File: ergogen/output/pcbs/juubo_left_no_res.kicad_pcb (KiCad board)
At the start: 2 copper layers, 145.6 x 125.5 mm, 40 parts

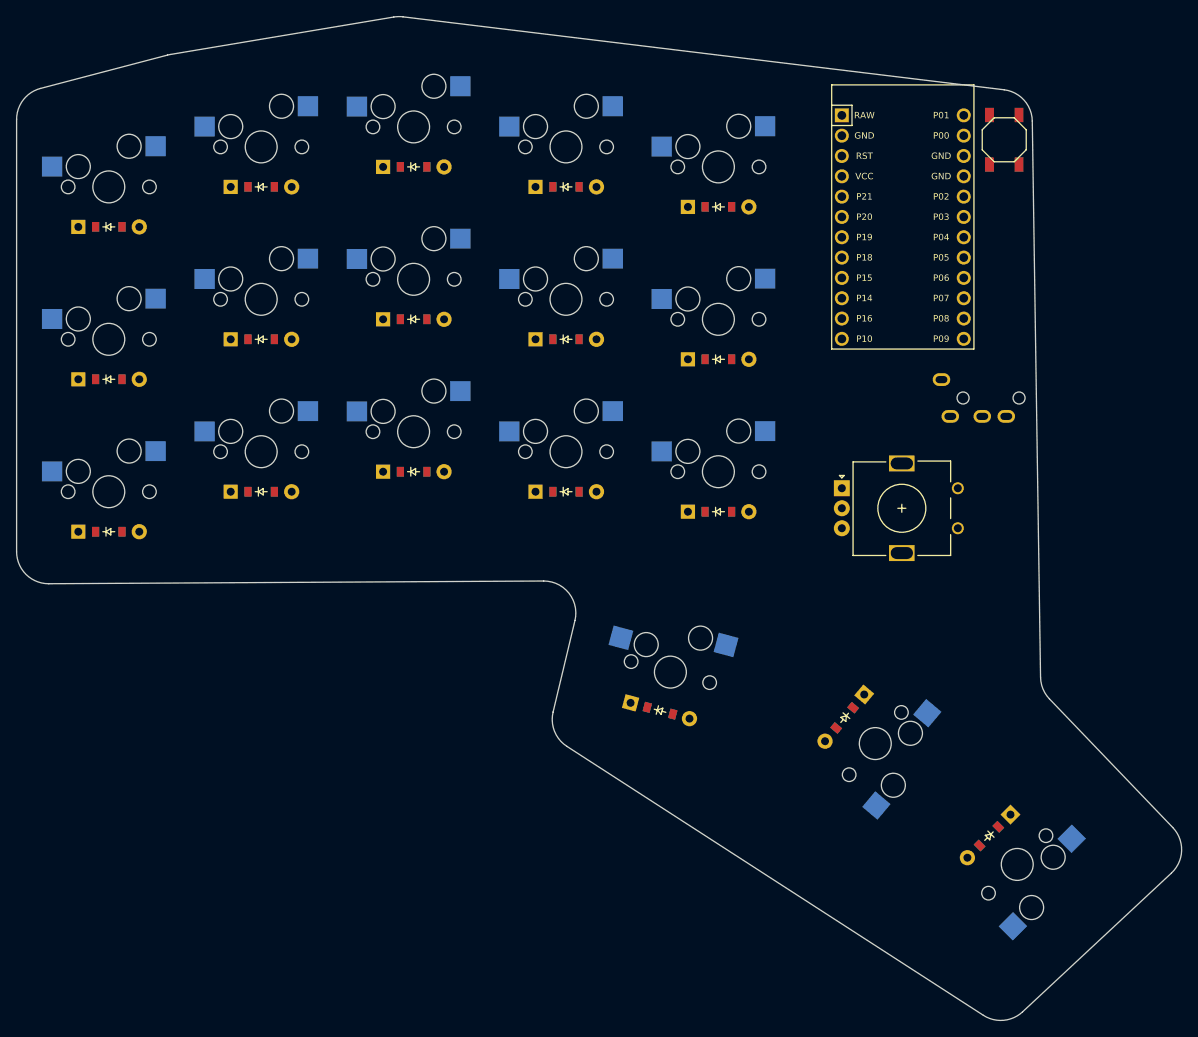
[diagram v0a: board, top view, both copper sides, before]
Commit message: Add mounting holes to ergogen-generated pcb
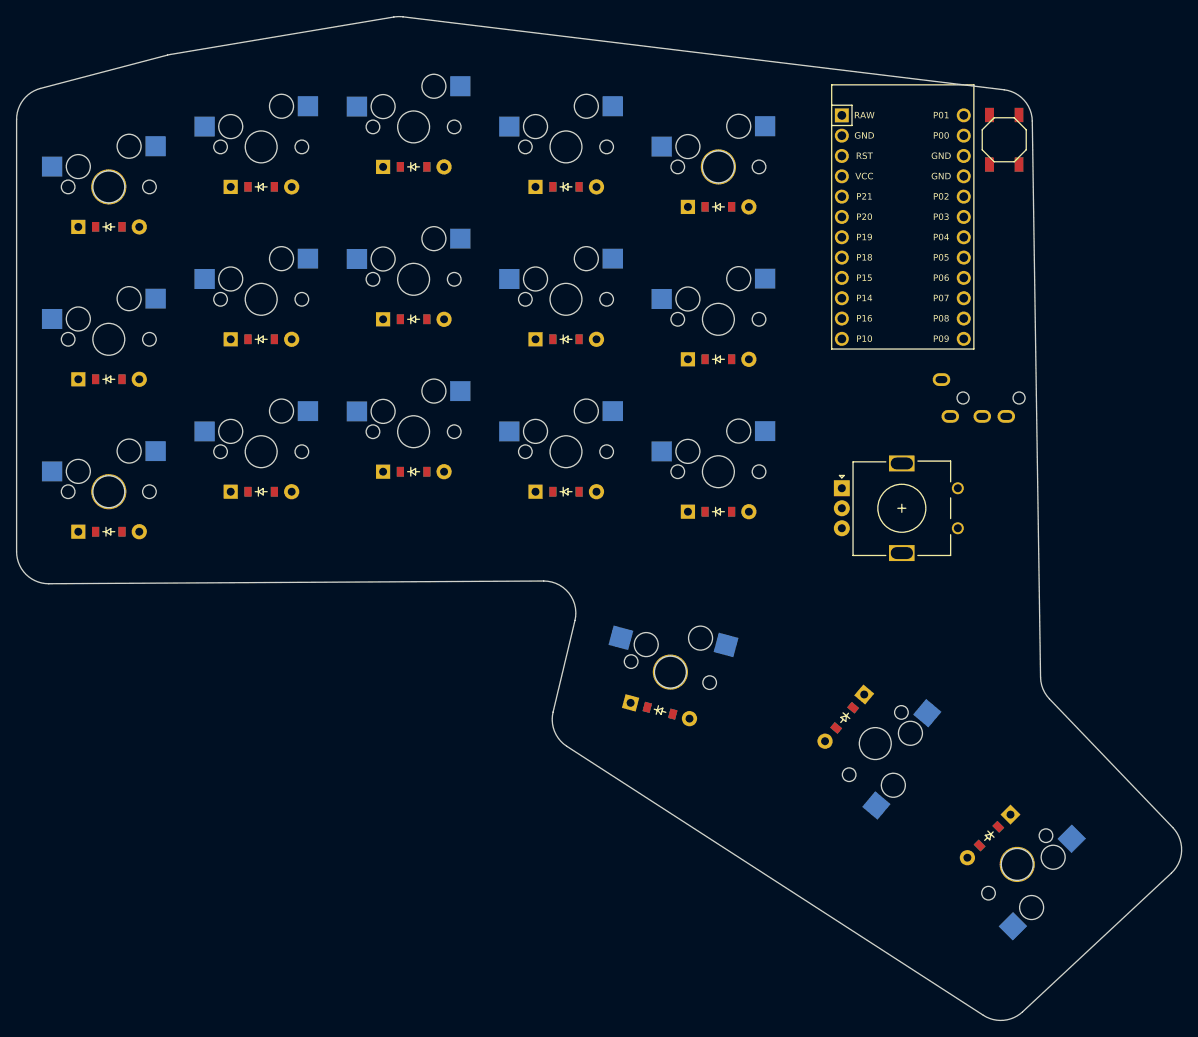
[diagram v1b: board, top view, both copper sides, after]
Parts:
- added _1: , MountingHole_2.2mm_M2_Pad_Via, F.Cu at (100.0, 61.9)
- added _2: , MountingHole_2.2mm_M2_Pad_Via, F.Cu at (176.2, 59.4)
- added _3: , MountingHole_2.2mm_M2_Pad_Via, F.Cu at (100.0, 100.0)
- added _4: , MountingHole_2.2mm_M2_Pad_Via, F.Cu at (170.2, 122.5)
- added _5: , MountingHole_2.2mm_M2_Pad_Via, F.Cu at (213.6, 146.6)
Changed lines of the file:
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@@
         (pad 4 thru_hole oval (at 0 3.2 -90) (size 1.6 2.2) (drill oval 0.9 1.5) (layers *.Cu *.Mask) (net 2 "GND"))
       )
+    (module "MountingHole_2.2mm_M2_Pad_Via" (version 20210722) (generator pcbnew) (layer "F.Cu")
+      (at 100 61.900000000000006 0)
+      (fp_text reference "_1" (at 0 -3.2) (layer "F.SilkS") hide
+        (effects (font (size 1 1) (thickness 0.15)))
+      )
+      (fp_circle (center 0 0) (end 2.45 0) (layer "F.CrtYd") (width 0.05) (fill none))
+      (pad "1" thru_hole circle locked (at 1.166726 1.166726) (size 0.7 0.7) (drill 0.4) (layers *.Cu *.Mask))
+      (pad "1" thru_hole circle locked (at 0 0) (size 4.4 4.4) (drill 2.2) (layers *.Cu *.Mask))
+      (pad "1" thru_hole circle locked (at 0 1.65) (size 0.7 0.7) (drill 0.4) (layers *.Cu *.Mask))
+      (pad "1" thru_hole circle locked (at 1.166726 -1.166726) (size 0.7 0.7) (drill 0.4) (layers *.Cu *.Mask))
+      (pad "1" thru_hole circle locked (at -1.65 0) (size 0.7 0.7) (drill 0.4) (layers *.Cu *.Mask))
+      (pad "1" thru_hole circle locked (at -1.166726 -1.166726) (size 0.7 0.7) (drill 0.4) (layers *.Cu *.Mask))
+      (pad "1" thru_hole circle locked (at -1.166726 1.166726) (size 0.7 0.7) (drill 0.4) (layers *.Cu *.Mask))
+      (pad "1" thru_hole circle locked (at 1.65 0) (size 0.7 0.7) (drill 0.4) (layers *.Cu *.Mask))
+      (pad "1" thru_hole circle locked (at 0 -1.65) (size 0.7 0.7) (drill 0.4) (layers *.Cu *.Mask))
+    )
+    (module "MountingHole_2.2mm_M2_Pad_Via" (version 20210722) (generator pcbnew) (layer "F.Cu")
+      (at 176.2 59.400000000000006 0)
+      (fp_text reference "_2" (at 0 -3.2) (layer "F.SilkS") hide
+        (effects (font (size 1 1) (thickness 0.15)))
+      )
+      (fp_circle (center 0 0) (end 2.45 0) (layer "F.CrtYd") (width 0.05) (fill none))
+      (pad "1" thru_hole circle locked (at 1.166726 1.166726) (size 0.7 0.7) (drill 0.4) (layers *.Cu *.Mask))
+      (pad "1" thru_hole circle locked (at 0 0) (size 4.4 4.4) (drill 2.2) (layers *.Cu *.Mask))
+      (pad "1" thru_hole circle locked (at 0 1.65) (size 0.7 0.7) (drill 0.4) (layers *.Cu *.Mask))
+      (pad "1" thru_hole circle locked (at 1.166726 -1.166726) (size 0.7 0.7) (drill 0.4) (layers *.Cu *.Mask))
+      (pad "1" thru_hole circle locked (at -1.65 0) (size 0.7 0.7) (drill 0.4) (layers *.Cu *.Mask))
+      (pad "1" thru_hole circle locked (at -1.166726 -1.166726) (size 0.7 0.7) (drill 0.4) (layers *.Cu *.Mask))
+      (pad "1" thru_hole circle locked (at -1.166726 1.166726) (size 0.7 0.7) (drill 0.4) (layers *.Cu *.Mask))
+      (pad "1" thru_hole circle locked (at 1.65 0) (size 0.7 0.7) (drill 0.4) (layers *.Cu *.Mask))
+      (pad "1" thru_hole circle locked (at 0 -1.65) (size 0.7 0.7) (drill 0.4) (layers *.Cu *.Mask))
+    )
+    (module "MountingHole_2.2mm_M2_Pad_Via" (version 20210722) (generator pcbnew) (layer "F.Cu")
+      (at 100 100 0)
+      (fp_text reference "_3" (at 0 -3.2) (layer "F.SilkS") hide
+        (effects (font (size 1 1) (thickness 0.15)))
+      )
+      (fp_circle (center 0 0) (end 2.45 0) (layer "F.CrtYd") (width 0.05) (fill none))
+      (pad "1" thru_hole circle locked (at 1.166726 1.166726) (size 0.7 0.7) (drill 0.4) (layers *.Cu *.Mask))
+      (pad "1" thru_hole circle locked (at 0 0) (size 4.4 4.4) (drill 2.2) (layers *.Cu *.Mask))
+      (pad "1" thru_hole circle locked (at 0 1.65) (size 0.7 0.7) (drill 0.4) (layers *.Cu *.Mask))
+      (pad "1" thru_hole circle locked (at 1.166726 -1.166726) (size 0.7 0.7) (drill 0.4) (layers *.Cu *.Mask))
+      (pad "1" thru_hole circle locked (at -1.65 0) (size 0.7 0.7) (drill 0.4) (layers *.Cu *.Mask))
+      (pad "1" thru_hole circle locked (at -1.166726 -1.166726) (size 0.7 0.7) (drill 0.4) (layers *.Cu *.Mask))
+      (pad "1" thru_hole circle locked (at -1.166726 1.166726) (size 0.7 0.7) (drill 0.4) (layers *.Cu *.Mask))
+      (pad "1" thru_hole circle locked (at 1.65 0) (size 0.7 0.7) (drill 0.4) (layers *.Cu *.Mask))
+      (pad "1" thru_hole circle locked (at 0 -1.65) (size 0.7 0.7) (drill 0.4) (layers *.Cu *.Mask))
+    )
+    (module "MountingHole_2.2mm_M2_Pad_Via" (version 20210722) (generator pcbnew) (layer "F.Cu")
+      (at 170.2 122.55 -15)
+      (fp_text reference "_4" (at 0 -3.2) (layer "F.SilkS") hide
+        (effects (font (size 1 1) (thickness 0.15)))
+      )
+      (fp_circle (center 0 0) (end 2.45 0) (layer "F.CrtYd") (width 0.05) (fill none))
+      (pad "1" thru_hole circle locked (at 1.166726 1.166726) (size 0.7 0.7) (drill 0.4) (layers *.Cu *.Mask))
+      (pad "1" thru_hole circle locked (at 0 0) (size 4.4 4.4) (drill 2.2) (layers *.Cu *.Mask))
+      (pad "1" thru_hole circle locked (at 0 1.65) (size 0.7 0.7) (drill 0.4) (layers *.Cu *.Mask))
+      (pad "1" thru_hole circle locked (at 1.166726 -1.166726) (size 0.7 0.7) (drill 0.4) (layers *.Cu *.Mask))
+      (pad "1" thru_hole circle locked (at -1.65 0) (size 0.7 0.7) (drill 0.4) (layers *.Cu *.Mask))
+      (pad "1" thru_hole circle locked (at -1.166726 -1.166726) (size 0.7 0.7) (drill 0.4) (layers *.Cu *.Mask))
+      (pad "1" thru_hole circle locked (at -1.166726 1.166726) (size 0.7 0.7) (drill 0.4) (layers *.Cu *.Mask))
+      (pad "1" thru_hole circle locked (at 1.65 0) (size 0.7 0.7) (drill 0.4) (layers *.Cu *.Mask))
+      (pad "1" thru_hole circle locked (at 0 -1.65) (size 0.7 0.7) (drill 0.4) (layers *.Cu *.Mask))
+    )
+    (module "MountingHole_2.2mm_M2_Pad_Via" (version 20210722) (generator pcbnew) (layer "F.Cu")
+      (at 213.55520369999996 146.590306 -135)
+      (fp_text reference "_5" (at 0 -3.2) (layer "F.SilkS") hide
+        (effects (font (size 1 1) (thickness 0.15)))
+      )
+      (fp_circle (center 0 0) (end 2.45 0) (layer "F.CrtYd") (width 0.05) (fill none))
+      (pad "1" thru_hole circle locked (at 1.166726 1.166726) (size 0.7 0.7) (drill 0.4) (layers *.Cu *.Mask))
+      (pad "1" thru_hole circle locked (at 0 0) (size 4.4 4.4) (drill 2.2) (layers *.Cu *.Mask))
+      (pad "1" thru_hole circle locked (at 0 1.65) (size 0.7 0.7) (drill 0.4) (layers *.Cu *.Mask))
+      (pad "1" thru_hole circle locked (at 1.166726 -1.166726) (size 0.7 0.7) (drill 0.4) (layers *.Cu *.Mask))
+      (pad "1" thru_hole circle locked (at -1.65 0) (size 0.7 0.7) (drill 0.4) (layers *.Cu *.Mask))
+      (pad "1" thru_hole circle locked (at -1.166726 -1.166726) (size 0.7 0.7) (drill 0.4) (layers *.Cu *.Mask))
+      (pad "1" thru_hole circle locked (at -1.166726 1.166726) (size 0.7 0.7) (drill 0.4) (layers *.Cu *.Mask))
+      (pad "1" thru_hole circle locked (at 1.65 0) (size 0.7 0.7) (drill 0.4) (layers *.Cu *.Mask))
+      (pad "1" thru_hole circle locked (at 0 -1.65) (size 0.7 0.7) (drill 0.4) (layers *.Cu *.Mask))
+    )
             (gr_line (start 88.475 107.50296162142857) (end 88.475 53.46061479002625) (angle 90) (layer Edge.Cuts) (width 0.15))
 (gr_line (start 91.45952643622041 49.591659728026144) (end 107.34956916334347 45.42104483901747) (angle 90) (layer Edge.Cuts) (width 0.15))
